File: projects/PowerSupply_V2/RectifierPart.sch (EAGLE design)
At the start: 13 parts, among them X1 OUT, X2 IN

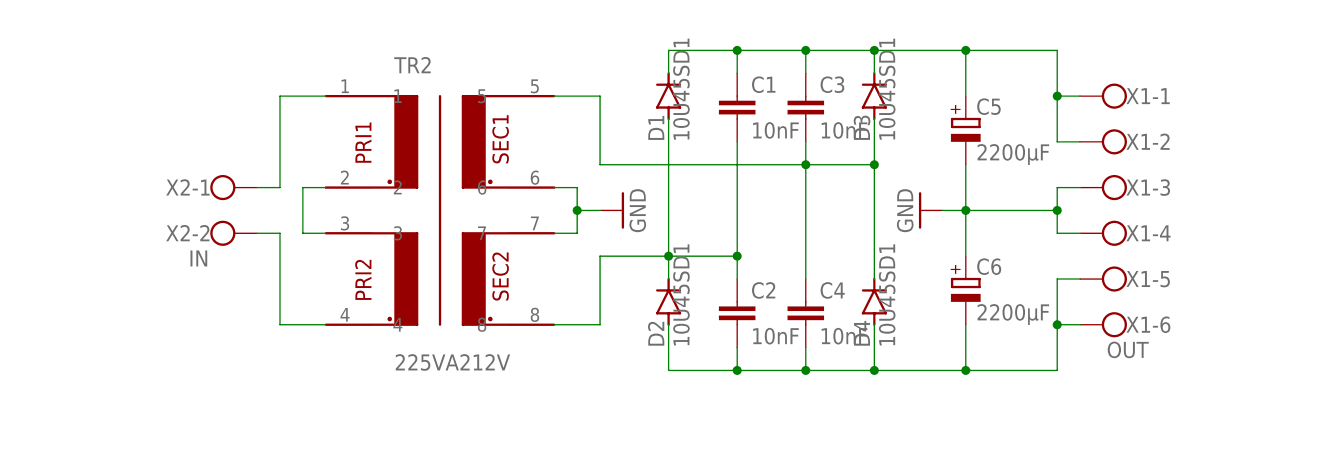
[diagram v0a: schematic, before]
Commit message: feat: power supply
changes:
- small fixes to rectifier capacity
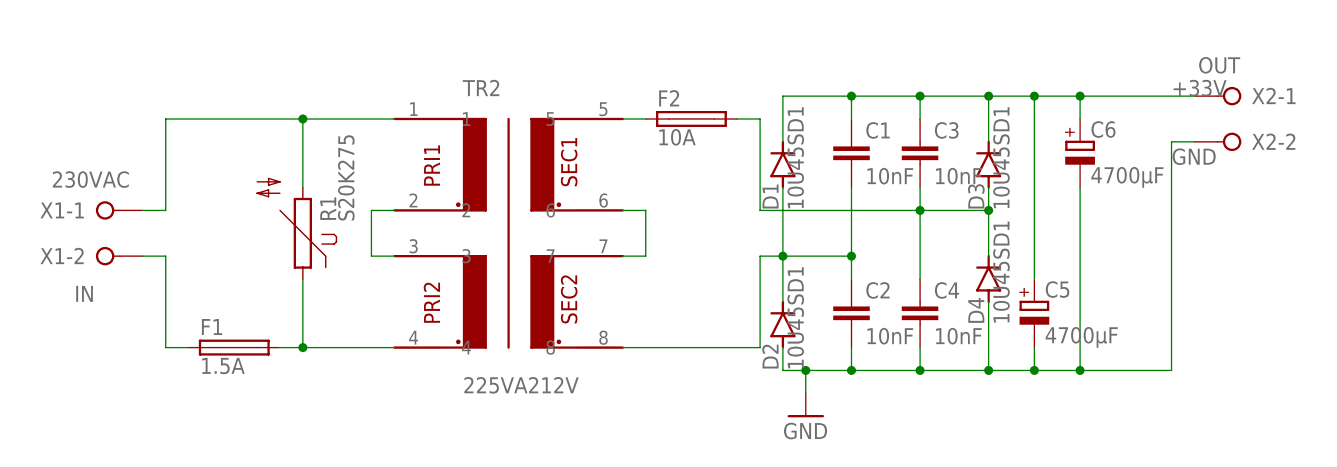
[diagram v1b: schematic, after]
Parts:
- added F1: 1.5A, fuse:SH22,5
- added F2: 10A, fuse:SH22,5
- added R1: S20K275, varistor:S20K275
- C5, C6: value 2200µF -> 4700µF
- X1: value OUT -> IN; device con-wago-500:W237-6 -> con-wago-508:W237-02P
- X2: value IN -> OUT; device con-wago-500:W237-102 -> con-wago-508:W237-02P
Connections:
- removed net N$7: TR2.1, X2-1.KL
- new net +33V: C1.1, C3.1, C5.+, C6.+, D1.C, D3.C, X2-1.KL
- new net 230VAC: R1.2, TR2.1, X1-1.KL
- new net N$8: TR2.6, TR2.7
- net GND: now also C2.2, C4.2, C6.-, D2.A, D4.A, X2-2.KL; no longer C6.+, TR2.6, TR2.7, X1-3.KL, X1-4.KL
- net N$1: now also F2.2; no longer TR2.5
- net N$2: now also F2.1, TR2.5; no longer C2.2, C4.2, C6.-, D2.A, D4.A, X1-5.KL, X1-6.KL
- net N$5: now also F1.1; no longer C1.1, C3.1, C5.+, D1.C, D3.C, X1-1.KL
- net N$6: now also F1.2, R1.1; no longer X2-2.KL
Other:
- moved on the sheet: C1, C2, C3, C4, C5, C6, D1, D2, D3, D4, TR2
